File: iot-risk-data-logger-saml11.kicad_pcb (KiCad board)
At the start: 2 copper layers, 51 x 51 mm, 36 parts, among them J1 Pickit 5 Conn, Q1 IRLML6401, U1 ATSAML11E16A-AU, U2 MMA8452QR1, U3 ST25DV04K, U4 OPT3001DNPR, U5 SHT30-DIS, U6 AT25SF041B-SSHD-T

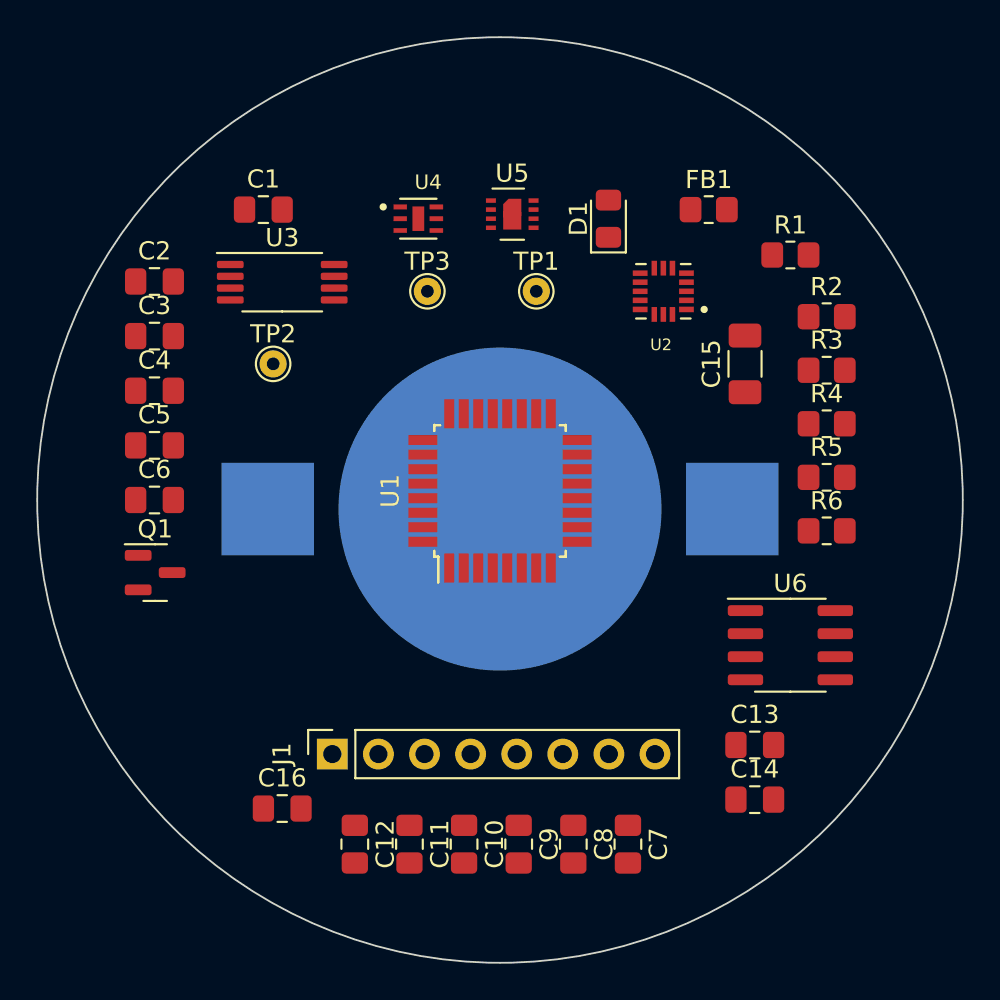
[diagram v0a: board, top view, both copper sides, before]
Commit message: DRAFT:replace saml11 by stm32l412, add USB
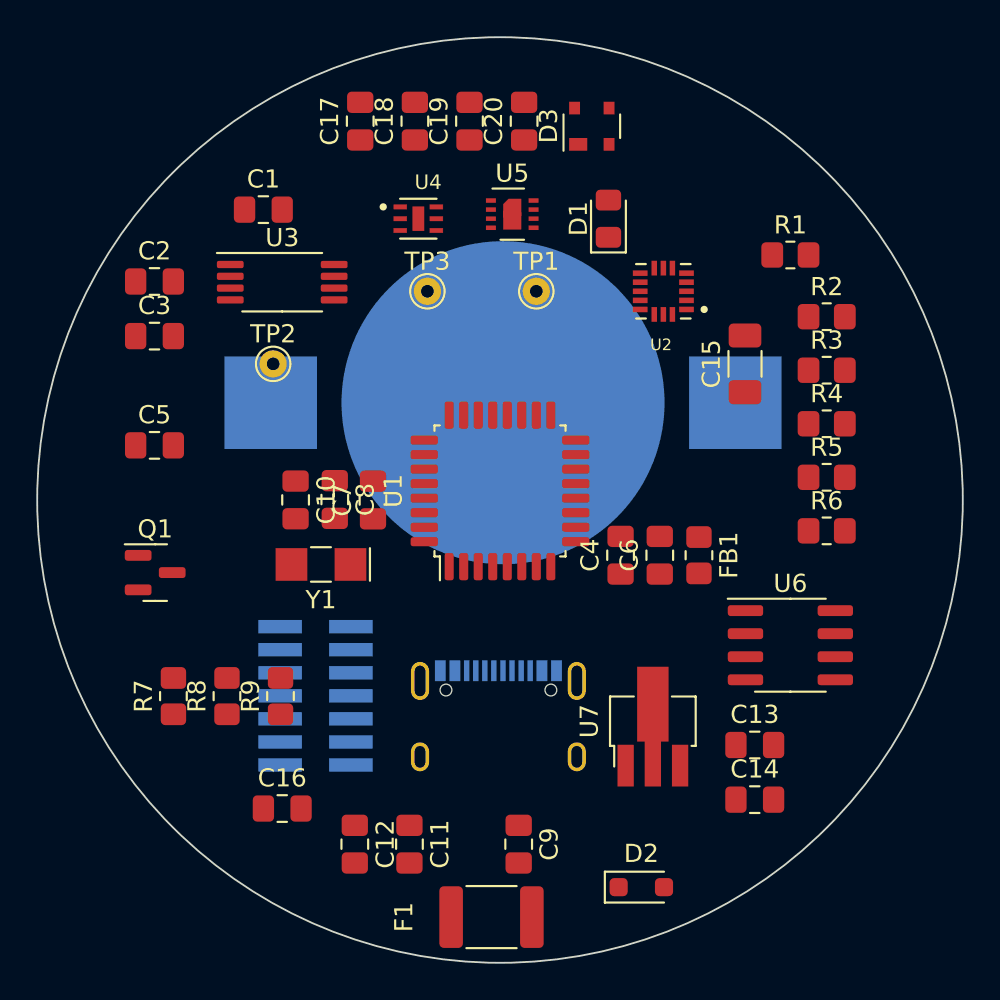
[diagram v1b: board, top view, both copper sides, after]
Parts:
- removed J1: Pickit 5 Conn, Connector_PinSocket_2.54mm:PinSocket_1x08_P2.54mm_Vertical
- added C17: 22p, Capacitor_SMD:C_0805_2012Metric_Pad1.18x1.45mm_HandSolder, F.Cu at (121.8, 66.1)
- added C18: 22p, Capacitor_SMD:C_0805_2012Metric_Pad1.18x1.45mm_HandSolder, F.Cu at (124.8, 66.1)
- added C19: 4n7, Capacitor_SMD:C_0805_2012Metric_Pad1.18x1.45mm_HandSolder, F.Cu at (127.8, 66.1)
- added C20: 10u, Capacitor_SMD:C_0805_2012Metric_Pad1.18x1.45mm_HandSolder, F.Cu at (130.8, 66.1)
- added D2: BAT60A, Diode_SMD:D_SOD-323_HandSoldering, F.Cu at (137.3, 108.3)
- added D3: PRTR5V0U2X, Package_TO_SOT_SMD:SOT-143, F.Cu at (134.6, 66.4)
- added F1: MSMF010 0.01A, Fuse:Fuse_1812_4532Metric_Pad1.30x3.40mm_HandSolder, F.Cu at (129.0, 110.0)
- added J2: Conn_ST_STDC14, Connector_PinHeader_1.27mm:PinHeader_2x07_P1.27mm_Vertical_SMD, B.Cu at (119.3, 97.8)
- added J3: USB Type-C, Connector_USB:USB_C_Receptacle_XKB_U262-16XN-4BVC11, B.Cu at (129.4, 100.1)
- added R7: 5k1, Resistor_SMD:R_0805_2012Metric_Pad1.20x1.40mm_HandSolder, F.Cu at (111.5, 97.8)
- added R8: 5k1, Resistor_SMD:R_0805_2012Metric_Pad1.20x1.40mm_HandSolder, F.Cu at (114.5, 97.8)
- added R9: 10k, Resistor_SMD:R_0805_2012Metric_Pad1.20x1.40mm_HandSolder, F.Cu at (117.4, 97.8)
- added U7: L78L33ABUTR, Package_TO_SOT_SMD:SOT-89-3_Handsoldering, F.Cu at (137.9, 99.2)
- added Y1: SC-32S32.768, Crystal:Crystal_SMD_EuroQuartz_EQ161-2Pin_3.2x1.5mm_HandSoldering, F.Cu at (119.6, 90.6)
- BT1: value 2032 Cell -> CR2032
- R2: value 10k -> 1M
- R6: value 100k -> 10k
- U1: value ATSAML11E16A-AU -> STM32L412K8Tx; footprint Package_QFP:TQFP-32_7x7mm_P0.8mm -> Package_QFP:LQFP-32_7x7mm_P0.8mm
- moved C6 28.0 mm to (138.3, 90.0), turned to 90 degrees
- moved C4 27.2 mm to (136.1, 90.0), turned to 90 degrees
- moved C7 23.6 mm to (122.5, 87.0), turned to 90 degrees
- moved C8 23.1 mm to (120.4, 87.0)
- moved C10 21.1 mm to (118.2, 87.0)
- moved FB1 19.1 mm to (140.5, 90.0), turned to -90 degrees
- moved BT1 5.86 mm to (129.7, 81.6)
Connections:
- net Net-(Q1-G) renamed +5V
- C10 pad 1: Net-(U1-VDDCORE) -> /VDDCODE
- C4 pad 1: Net-(U1-VDDANA) -> /VDDANA
- C6 pad 1: Net-(U1-VDDANA) -> /VDDANA
- C7 pad 1: Net-(U1-VDDIO) -> unconnected-(C7-Pad1)
- C8 pad 1: Net-(U1-VDDCORE) -> /VDDCODE
- FB1 pad 2: Net-(U1-VDDANA) -> /VDDANA
- Q1 pad 3: Net-(BT1-+) -> Net-(Q1-D)
- R2 pad 1: +3V0 -> Net-(D3-GND)
- R2 pad 2: _RESET -> GND
- R6 pad 2: GND -> USB_VBUS_SENSE
- U1 pad 10: GND -> unconnected-(U1-PA4-Pad10)
- U1 pad 11: MOSI -> unconnected-(U1-PA5-Pad11)
- U1 pad 12: SCK -> unconnected-(U1-PA6-Pad12)
- U1 pad 13: _FLASH_CS -> unconnected-(U1-PA7-Pad13)
- U1 pad 14: MISO -> unconnected-(U1-PB0-Pad14)
- U1 pad 16: unconnected-(U1-PA15/XOUT-Pad16) -> GND
- U1 pad 17: SDA -> unconnected-(U1-VDD-Pad17)
- U1 pad 18: SCL -> unconnected-(U1-PA8-Pad18)
- U1 pad 19: _NFC_INT -> unconnected-(U1-PA9-Pad19)
- U1 pad 20: _LIGHT_INT -> unconnected-(U1-PA10-Pad20)
- U1 pad 21: IMU_INT1 -> unconnected-(U1-PA11-Pad21)
- U1 pad 22: IMU_INT2 -> unconnected-(U1-PA12-Pad22)
- U1 pad 23: TEMP_INT -> unconnected-(U1-PA13-Pad23)
- U1 pad 24: _TEMP_RESET -> unconnected-(U1-PA14-Pad24)
- U1 pad 26: _RESET -> unconnected-(U1-PB3-Pad26)
- U1 pad 27: Net-(U1-VDDCORE) -> unconnected-(U1-PB4-Pad27)
- U1 pad 28: GND -> unconnected-(U1-PB5-Pad28)
- U1 pad 30: Net-(U1-VDDIO) -> unconnected-(U1-PB7-Pad30)
- U1 pad 31: SWDCLK -> unconnected-(U1-PH3-Pad31)
- U1 pad 32: SWDIO -> GND
- U1 pad 4: unconnected-(U1-PA03/VREFA-Pad4) -> _RESET
- U1 pad 6: _LED -> unconnected-(U1-PA0-Pad6)
- U1 pad 9: Net-(U1-VDDANA) -> unconnected-(U1-PA3-Pad9)
